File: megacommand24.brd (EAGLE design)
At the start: 109.8 x 83.8 mm, 68 parts, among them IC1 74HC573N, IC2 74LS165N, IC3 74LS165N, IC4 HC4050, J1 DCJ0202, SW1 PEC11, SW2 PEC11, SW3 PEC11, SW4 PEC11

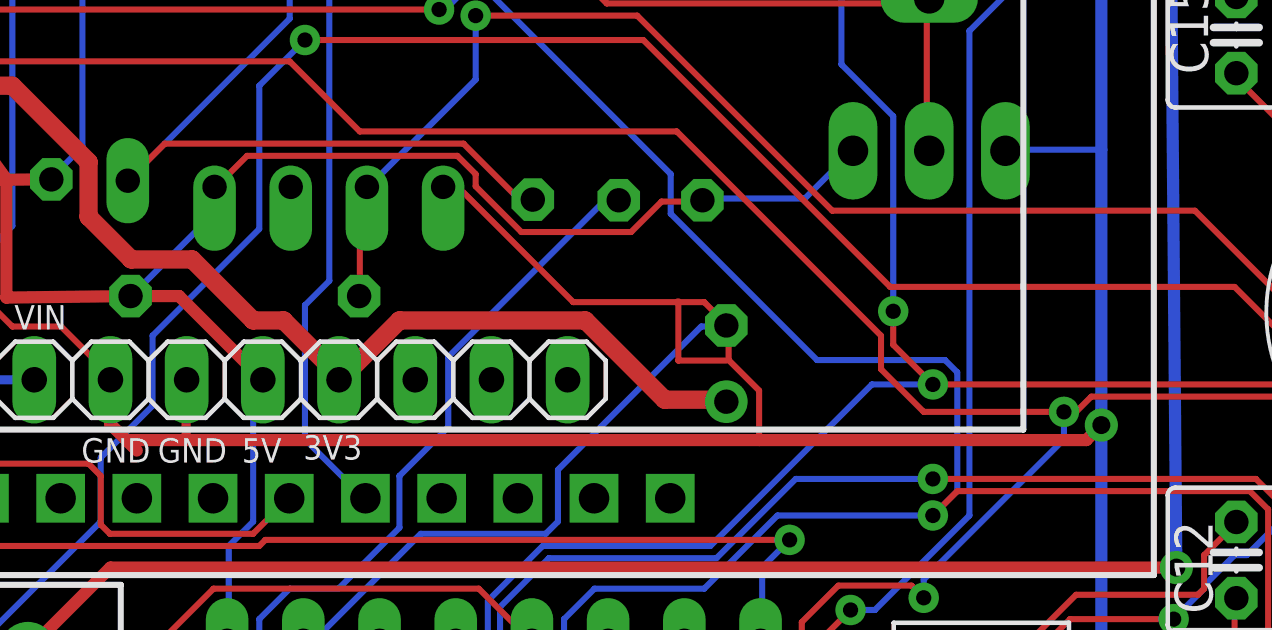
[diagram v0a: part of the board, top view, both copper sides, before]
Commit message: Fix for GND rail
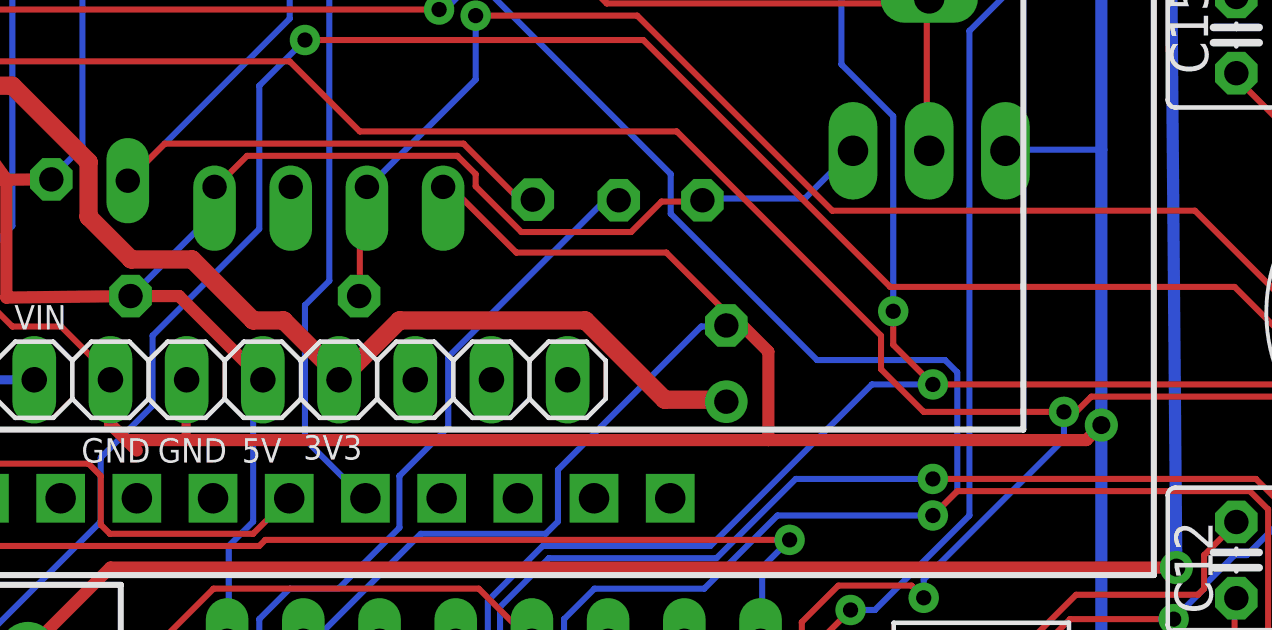
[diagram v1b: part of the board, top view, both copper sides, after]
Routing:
- net GND: track 716.5 -> 713.7 mm
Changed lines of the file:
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@@
 <wire x1="93.5" y1="58.928" x2="93.5" y2="49.75" width="0.4064" layer="16"/>
 <wire x1="93.5" y1="49.75" x2="93" y2="49.25" width="0.4064" layer="1"/>
-<wire x1="93" y1="49.25" x2="82.0928" y2="49.25" width="0.4064" layer="1"/>
-<wire x1="82.0928" y1="49.25" x2="62.992" y2="49.25" width="0.4064" layer="1"/>
+<wire x1="93" y1="49.25" x2="82.4" y2="49.25" width="0.4064" layer="1"/>
+<wire x1="82.4" y1="49.25" x2="62.992" y2="49.25" width="0.4064" layer="1"/>
 <wire x1="62.992" y1="49.25" x2="61" y2="49.25" width="0.4064" layer="1"/>
 <wire x1="61" y1="49.25" x2="60.47" y2="49.78" width="0.4064" layer="1"/>
@@
 <wire x1="66.8528" y1="42.4688" x2="66.9" y2="42.56" width="0.2032" layer="16"/>
 <wire x1="59.0296" y1="35.7632" x2="58.98" y2="35.75" width="0.2032" layer="16"/>
-<wire x1="72.136" y1="57.6072" x2="71.628" y2="57.6072" width="0.2032" layer="1"/>
-<wire x1="75.8952" y1="53.848" x2="72.136" y2="57.6072" width="0.2032" layer="1"/>
-<wire x1="80.264" y1="53.848" x2="79.383546875" y2="53.848" width="0.2032" layer="1"/>
-<wire x1="79.383546875" y1="53.848" x2="75.8952" y2="53.848" width="0.2032" layer="1"/>
-<wire x1="80.9752" y1="53.1368" x2="80.264" y2="53.848" width="0.2032" layer="1"/>
-<wire x1="71.628" y1="57.6072" x2="71.56" y2="57.69" width="0.2032" layer="1"/>
-<wire x1="80.9752" y1="53.1368" x2="81" y2="53.07" width="0.2032" layer="1"/>
 <wire x1="67.2592" y1="42.5704" x2="66.9544" y2="42.5704" width="0.2032" layer="16"/>
 <wire x1="70.8152" y1="46.1264" x2="67.2592" y2="42.5704" width="0.2032" layer="16"/>
@@
 <wire x1="30.7848" y1="47.244" x2="30.87" y2="47.31" width="0.2032" layer="16"/>
 <wire x1="25.7048" y1="42.164" x2="25.73" y2="42" width="0.2032" layer="16"/>
-<wire x1="81.0768" y1="51.9176" x2="81.0768" y2="53.0352" width="0.2032" layer="1"/>
-<wire x1="82.0928" y1="50.9016" x2="81.0768" y2="51.9176" width="0.2032" layer="1"/>
-<wire x1="82.0928" y1="49.25" x2="82.0928" y2="50.9016" width="0.2032" layer="1"/>
 <wire x1="81.0768" y1="53.0352" x2="81" y2="53.07" width="0.2032" layer="1"/>
-<wire x1="79.383546875" y1="53.848" x2="79.4" y2="53.848" width="0.254" layer="1"/>
-<wire x1="79.4" y1="53.848" x2="79.4" y2="51.9" width="0.204" layer="1"/>
-<wire x1="79.4" y1="51.9" x2="81" y2="51.9" width="0.204" layer="1"/>
 <contactref element="J1" pad="1"/>
 <wire x1="93.5" y1="69.655" x2="94.555" y2="69.655" width="0.4064" layer="16"/>
@@
 <wire x1="100.6856" y1="67.4076" x2="95.8" y2="67.4076" width="0.3048" layer="1"/>
 <wire x1="95.8" y1="67.4076" x2="95.8" y2="70.9" width="0.3048" layer="1"/>
+<wire x1="82.4" y1="49.25" x2="82.4" y2="52.2" width="0.4064" layer="1"/>
+<wire x1="82.4" y1="52.2" x2="81.53" y2="53.07" width="0.4064" layer="1"/>
+<wire x1="81.53" y1="53.07" x2="81" y2="53.07" width="0.4064" layer="1"/>
+<wire x1="74" y1="55.5" x2="72" y2="57.5" width="0.2032" layer="1"/>
+<wire x1="79" y1="55.5" x2="74" y2="55.5" width="0.2032" layer="1"/>
+<wire x1="81" y1="53.5" x2="79" y2="55.5" width="0.2032" layer="1"/>
+<wire x1="72" y1="57.5" x2="71.56" y2="57.69" width="0.2032" layer="1"/>
+<wire x1="81" y1="53.5" x2="81" y2="53.07" width="0.2032" layer="1"/>
 </signal>
 <signal name="AREF">
